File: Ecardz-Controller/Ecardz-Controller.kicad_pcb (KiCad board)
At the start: 4 copper layers, 189 x 115 mm, 165 parts, among them IC1 ST25R3916B-AQWT, J1 MEM2061-01-188-00-A, J2 Conn_01x04, J3 Conn_01x05, J4 Conn_01x09, J5 Conn_01x01, J6 Conn_01x24, J7 Conn_01x02, J8 Conn_01x04, J9 Conn_01x04, Q1 NMOS, U1 STM32G0C1RETx, U2 TPS62160DSG, U3 MIC5504-3.3YM5, U4 CP2110-F02-GM1, Y1 XRCGB27M120F3M00R0

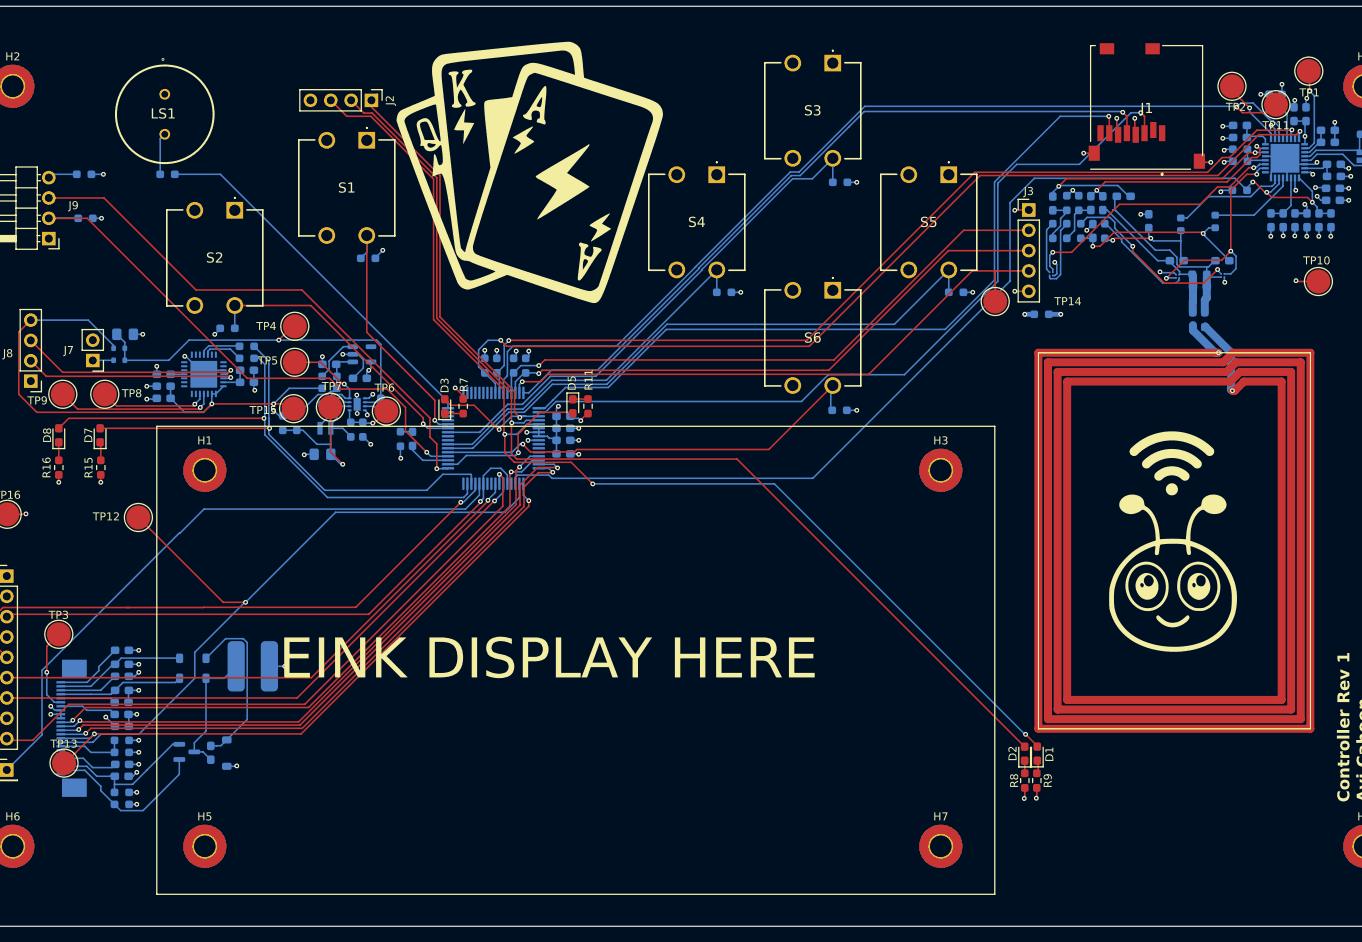
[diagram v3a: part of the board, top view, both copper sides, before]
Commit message: updates based on review
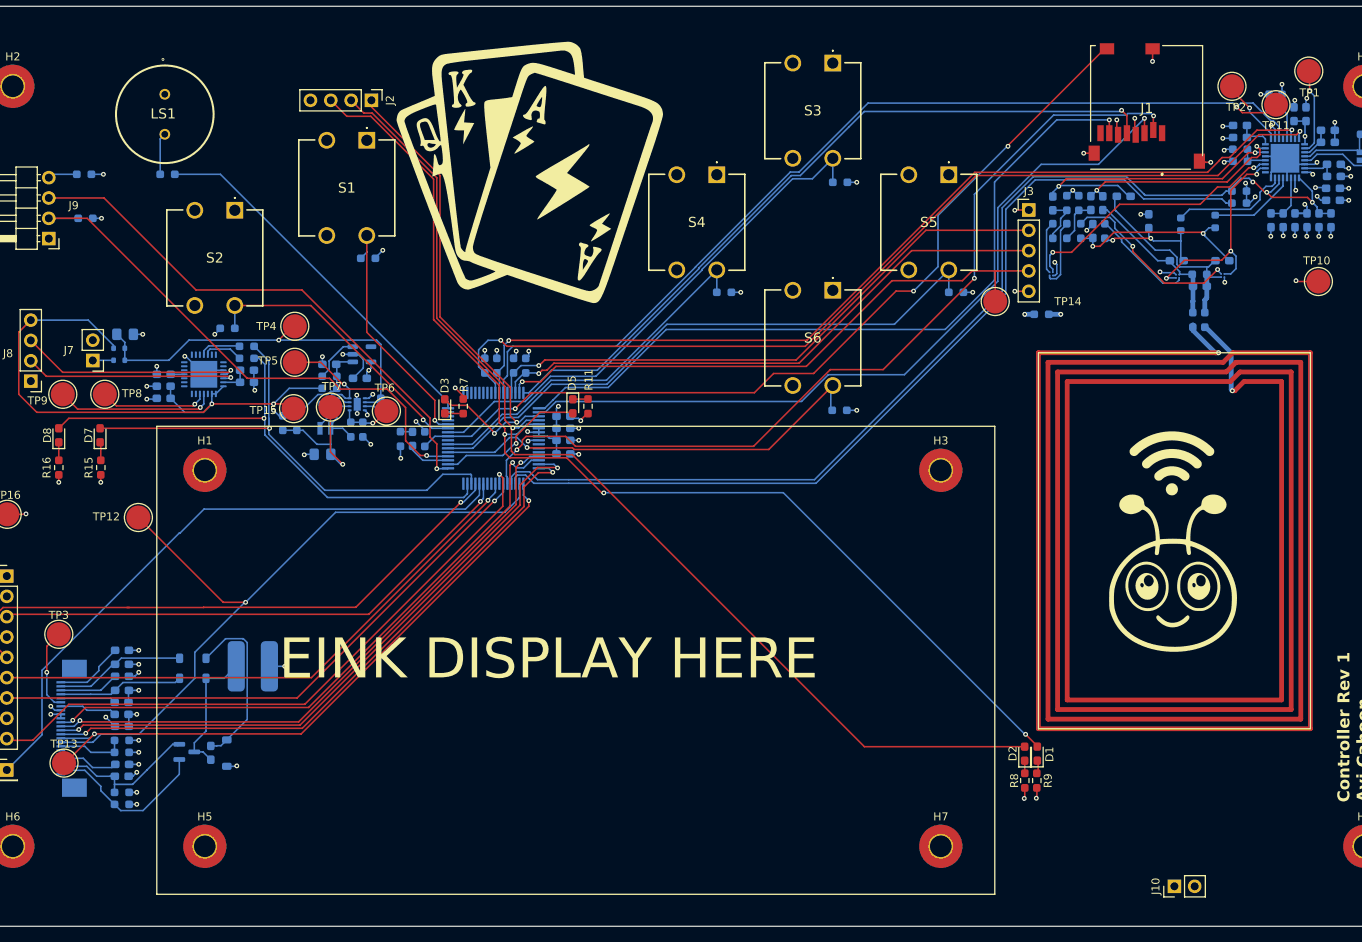
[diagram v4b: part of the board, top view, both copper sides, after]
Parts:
- added J10: Conn_01x02, Connector_PinHeader_2.54mm:PinHeader_1x02_P2.54mm_Vertical, F.Cu at (205.2, 200.0)
- added R50: 10k, Resistor_SMD:R_0603_1608Metric_Pad0.98x0.95mm_HandSolder, B.Cu at (111.5, 144.1)
- added R51: 0, Resistor_SMD:R_0603_1608Metric_Pad0.98x0.95mm_HandSolder, B.Cu at (213.3, 114.6)
- moved R2 0.12 mm to (213.3, 113.1), turned to 180 degrees
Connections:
- C6 pad 2: /MCU/NFC_I_SENSE -> /MCU/NFC_I_SENSE_P
- C8 pad 2: /MCU/NFC_I_SENSE -> /MCU/NFC_I_SENSE_P
- IC1 pad 14: /MCU/NFC_I_SENSE -> /MCU/NFC_I_SENSE_P
- IC1 pad 9: /MCU/NFC_I_SENSE -> /MCU/NFC_I_SENSE_P
- J1 pad CD1: unconnected-(J1-CARD_DETECT_1-PadCD1) -> GND
- J1 pad CD2: unconnected-(J1-CARD_DETECT_2-PadCD2) -> /MCU/SD_CARD_DETECT
- J4 pad 3: /MCU/SPI_LCD_CS -> /INTERFACE/SPI_LCD_CS
- R2 pad 2: /MCU/NFC_I_SENSE -> /MCU/NFC_I_SENSE_P
- U1 pad 19: /MCU/NFC_I_SENSE -> /MCU/NFC_I_SENSE_N
- U1 pad 20: unconnected-(U1-PA3-Pad20) -> /MCU/NFC_I_SENSE_P
- U1 pad 21: /MCU/SPI_LCD_CS -> /MCU/SD_CS
- U1 pad 27: /MCU/SPI_LCD_CS -> /INTERFACE/SPI_LCD_CS
- U1 pad 41: unconnected-(U1-PD9-Pad41) -> /MCU/SD_CARD_DETECT
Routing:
- net /MCU/NFC_I_SENSE_P: track 0.00 -> 137.1 mm, vias 0 -> 3
- net /MCU/NFC_I_SENSE: track 134.8 -> 0.00 mm, vias 3 -> 0
- net /MCU/NFC_I_SENSE_N: track 0.00 -> 114.0 mm
- net /MCU/SD_CS: track 0.00 -> 111.2 mm, vias 0 -> 3
- net /MCU/SD_CARD_DETECT: track 0.00 -> 109.9 mm, vias 0 -> 3
- net /MCU/SPI_LCD_CS: track 74.3 -> 0.00 mm, vias 1 -> 0
- net /INTERFACE/SPI_LCD_CS: track 0.00 -> 68.4 mm, vias 0 -> 1
- net VDD_NFC: track 21.7 -> 25.5 mm, vias 11 -> 12
- net /MCU/SD_MOSI: track 100.2 -> 97.7 mm
- net +3V3: track 30.3 -> 31.9 mm, vias 15 -> 16
- net GND: track 125.3 -> 126.7 mm, vias 77 -> 78
- net /INTERFACE/SDA: track 75.8 -> 77.0 mm
- net /MCU/LED_DISPLAY_R: track 19.7 -> 18.8 mm
- net /INTERFACE/BUTTON7: track 67.6 -> 68.3 mm
- net /MCU/SD_MISO: track 95.7 -> 95.1 mm
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
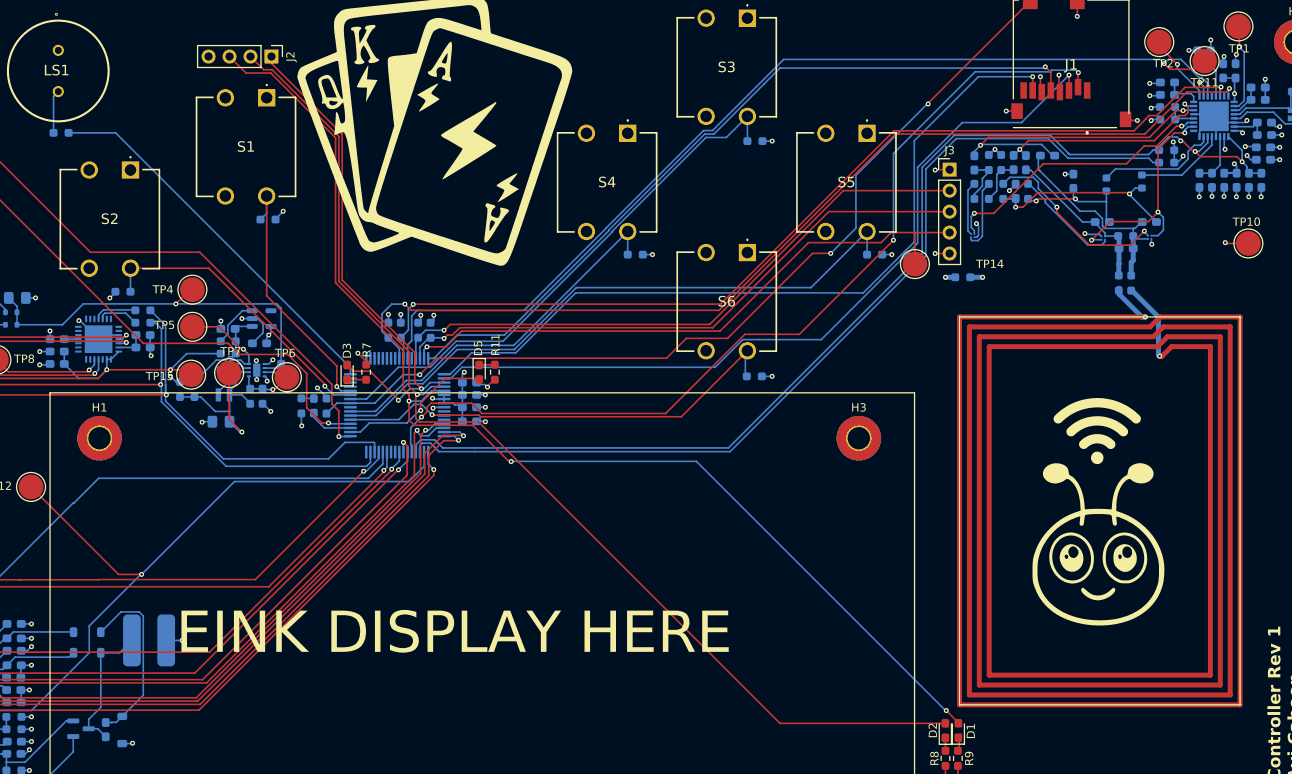
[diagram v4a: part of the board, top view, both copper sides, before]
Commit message: added current sense resistor and modified buzzer circuit
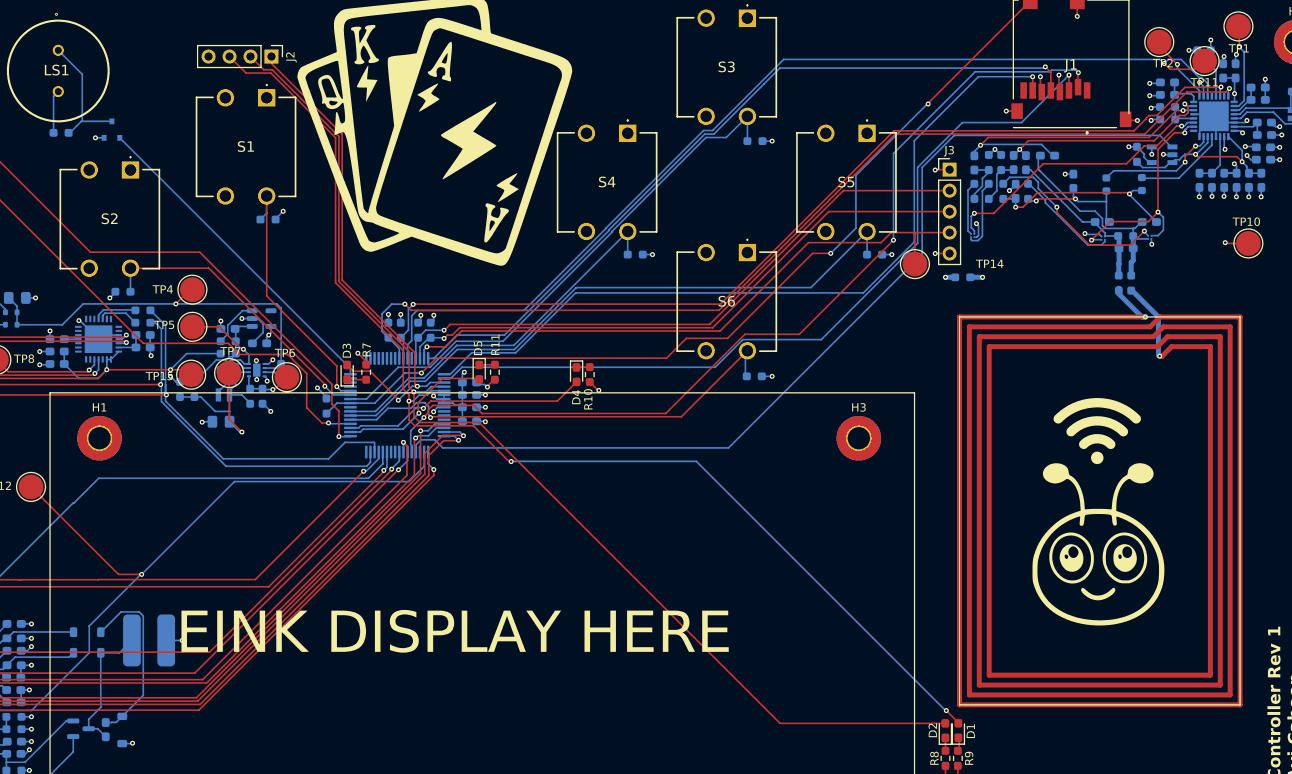
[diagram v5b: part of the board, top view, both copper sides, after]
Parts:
- removed R51: 0, Resistor_SMD:R_0603_1608Metric_Pad0.98x0.95mm_HandSolder
- added IC2: INA180A2IDBVR, samacsys:SOT95P280X145-5N, B.Cu at (212.8, 113.7)
- added Q2: TMBT3904,LM, samacsys:TMBT3904LM, B.Cu at (85.5, 110.6)
- D4, R10: moved to F.Cu
- moved R10 35.1 mm to (143.4, 140.3)
- moved D4 32.1 mm to (141.8, 140.3)
- moved R2 3.63 mm to (209.7, 113.6), turned to -90 degrees
- moved L3 0.30 mm to (210.3, 117.2)
- turned R19 to 0 degrees
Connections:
- C6 pad 2: /MCU/NFC_I_SENSE_P -> Net-(IC1-VDD_DR)
- C8 pad 2: /MCU/NFC_I_SENSE_P -> Net-(IC1-VDD_DR)
- IC1 pad 14: /MCU/NFC_I_SENSE_P -> Net-(IC1-VDD_DR)
- IC1 pad 9: /MCU/NFC_I_SENSE_P -> Net-(IC1-VDD_DR)
- LS1 pad 1: GND -> Net-(Q2-C)
- LS1 pad 2: Net-(LS1-Pad2) -> +3V3
- R19 pad 1: /INTERFACE/BUZZER -> +3V3
- R19 pad 2: Net-(LS1-Pad2) -> Net-(Q2-C)
- R2 pad 2: /MCU/NFC_I_SENSE_P -> Net-(IC1-VDD_DR)
- U1 pad 19: /MCU/NFC_I_SENSE_N -> unconnected-(U1-PA2-Pad19)
- U1 pad 20: /MCU/NFC_I_SENSE_P -> /MCU/NFC_I_SENSE
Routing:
- net /MCU/NFC_I_SENSE_P: track 137.1 -> 0.00 mm, vias 3 -> 0
- net /MCU/NFC_I_SENSE: track 0.00 -> 115.5 mm
- net /MCU/NFC_I_SENSE_N: track 114.0 -> 0.00 mm
- net Net-(IC1-VDD_DR): track 0.00 -> 24.7 mm, vias 0 -> 2
- net /MCU/LED_DISPLAY_B: track 5.49 -> 29.9 mm, vias 0 -> 1
- net Net-(Q2-C): track 0.00 -> 15.6 mm
- net /INTERFACE/BUZZER: track 46.7 -> 40.3 mm
- net +3V3: track 31.9 -> 37.3 mm
- net Net-(LS1-Pad2): track 5.24 -> 0.00 mm
- net GND: track 126.7 -> 129.0 mm, vias 78 -> 80
- net /INTERFACE/SDA: track 77.0 -> 75.9 mm
- net /INTERFACE/BUTTON6: track 56.0 -> 56.9 mm
- net /MCU/SD_CS: track 111.2 -> 110.7 mm
- net VDD_NFC: track 25.5 -> 25.0 mm
- net /MCU/LED_DEBUG_B: track 63.3 -> 62.8 mm
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
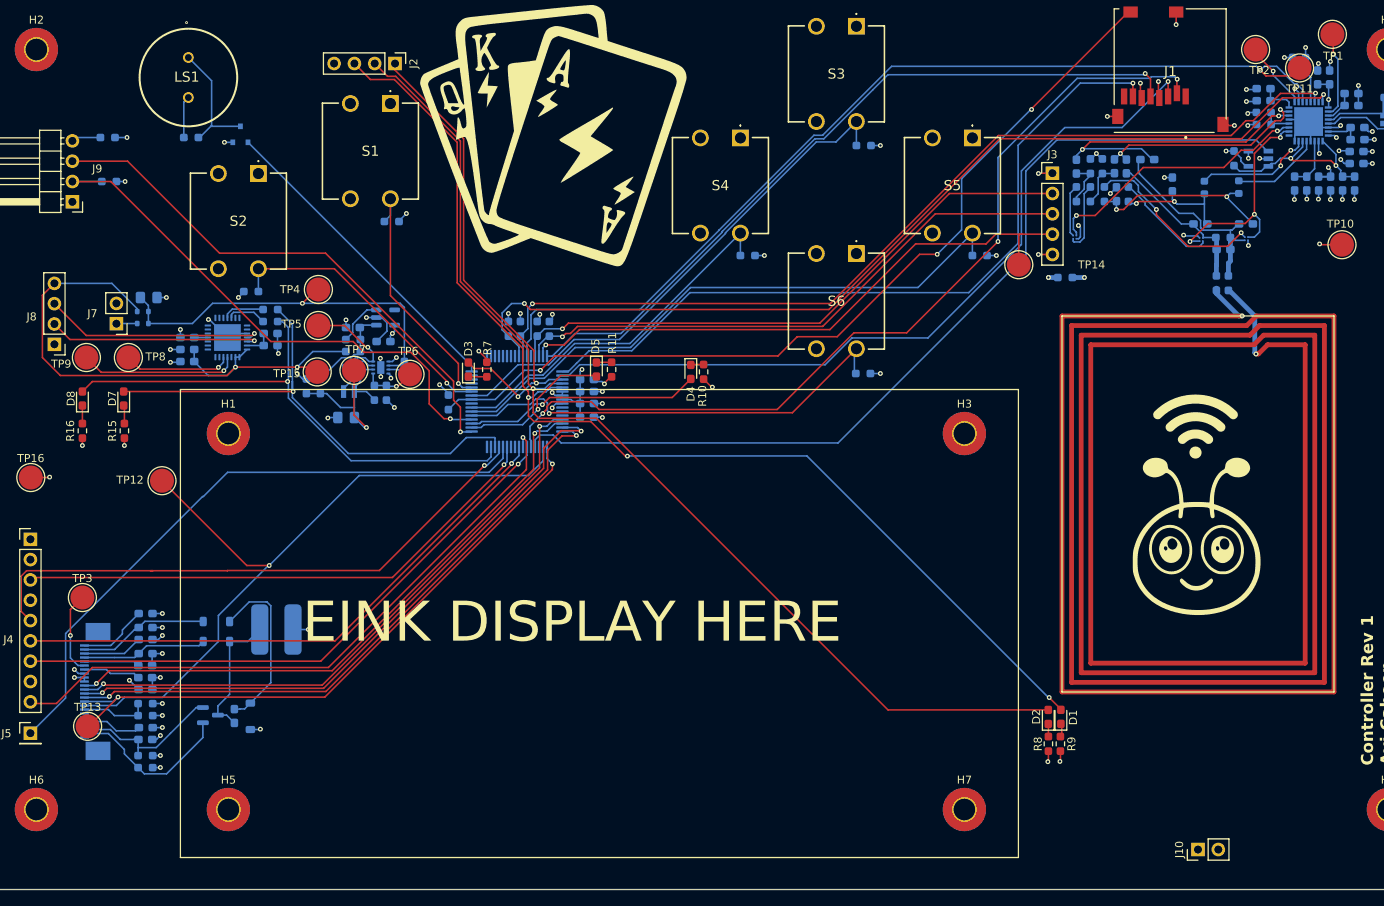
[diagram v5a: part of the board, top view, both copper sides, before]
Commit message: updated layout for new mcu pin assignments
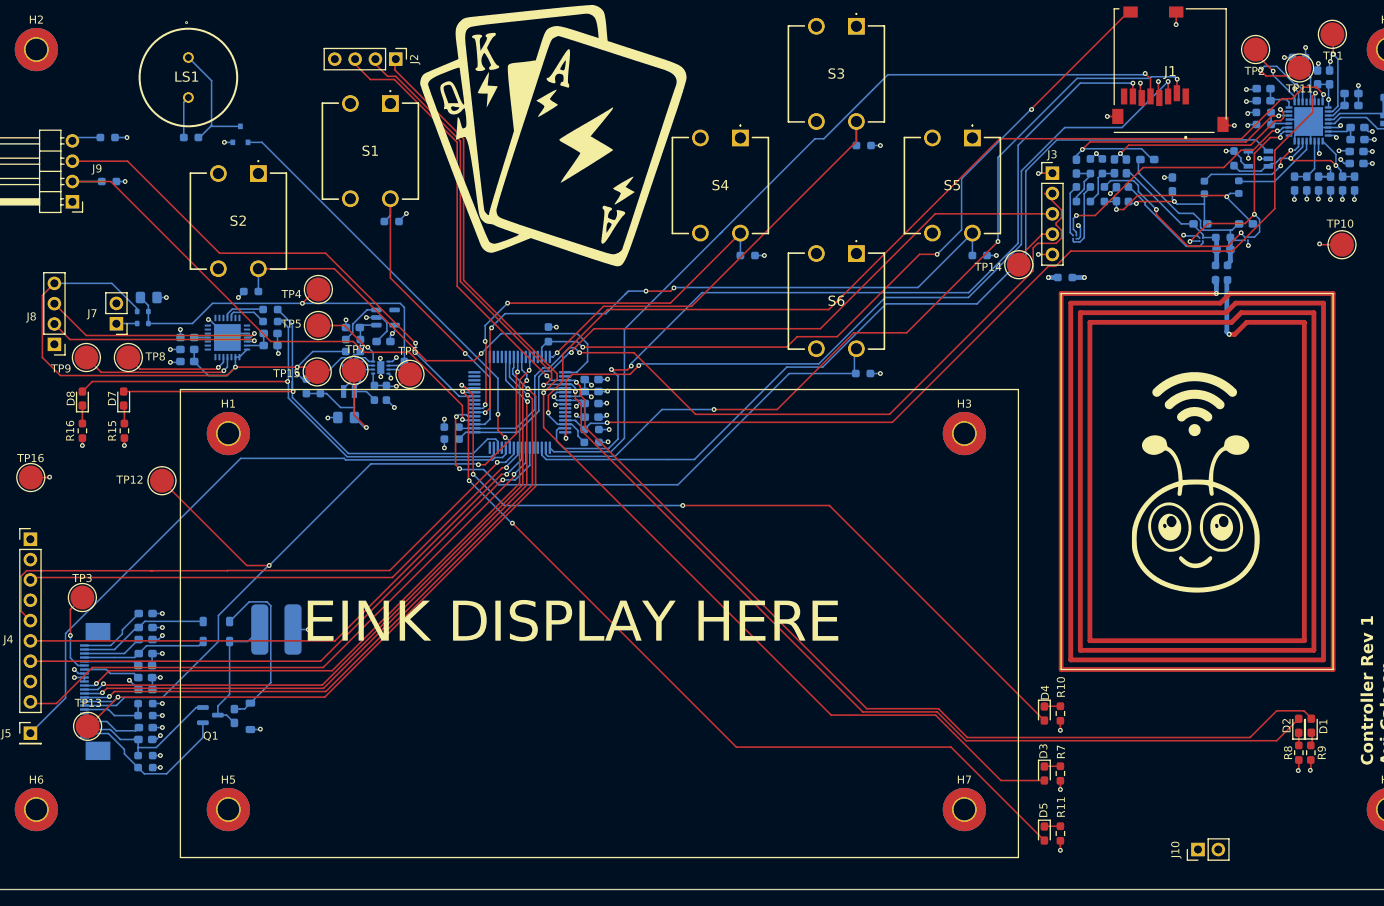
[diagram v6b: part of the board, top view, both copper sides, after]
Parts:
- moved D3 87.9 mm to (186.0, 190.5), turned to -90 degrees
- moved R7 87.7 mm to (188.0, 190.5), turned to -90 degrees
- moved R11 80.7 mm to (188.0, 198.0)
- moved D5 80.6 mm to (186.0, 198.0)
- moved R10 61.8 mm to (188.0, 183.0)
- moved D4 61.5 mm to (186.0, 183.0)
- moved R8 31.3 mm to (217.8, 187.9)
- moved R9 31.3 mm to (219.3, 187.9)
- moved D1 31.3 mm to (219.4, 184.5)
- moved D2 31.3 mm to (217.8, 184.5)
- moved R17 18.4 mm to (111.9, 148.7), turned to 0 degrees
- moved R14 17.6 mm to (129.4, 149.1), turned to 180 degrees
- moved R18 16.3 mm to (111.9, 147.2), turned to 0 degrees
- moved R13 15.4 mm to (129.4, 147.5), turned to 180 degrees
- moved R50 15.1 mm to (124.0, 135.6)
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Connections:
- IC1 pad 27: /MCU/NFC_BUSY -> /MCU/NFC_A_BUSY
- IC1 pad 30: /MCU/I2C_NFC_SCL -> /MCU/NFC_A_SCL
- IC1 pad 32: /MCU/I2C_NFC_SDA -> /MCU/NFC_A_SDA
- J4 pad 3: /INTERFACE/SPI_LCD_CS -> /MCU/SPI_LCD_CS
- J4 pad 5: /INTERFACE/SPI_LCD_DC -> /MCU/SPI_LCD_DC
- R13 pad 2: /MCU/I2C_NFC_SCL -> /MCU/NFC_A_SCL
- R14 pad 2: /MCU/I2C_NFC_SDA -> /MCU/NFC_A_SDA
- TP11 pad 1: /MCU/NFC_BUSY -> /MCU/NFC_A_BUSY
- U1 pad 1: /MCU/SD_MISO -> /INTERFACE/BUTTON2
- U1 pad 13: /INTERFACE/SCL -> /MCU/NFC_A_SCL
- U1 pad 14: /INTERFACE/SDA -> /MCU/NFC_A_SDA
- U1 pad 15: /INTERFACE/CS# -> /MCU/SD_MISO
- U1 pad 16: /INTERFACE/D/C# -> /MCU/SD_MOSI
- U1 pad 17: /INTERFACE/RES# -> /MCU/SD_SCK
- U1 pad 18: /INTERFACE/BUSY -> /MCU/SD_CS
- U1 pad 19: unconnected-(U1-PA2-Pad19) -> /MCU/NFC_I_SENSE
- U1 pad 2: /MCU/SD_MOSI -> unconnected-(U1-PC12-Pad2)
- U1 pad 20: /MCU/NFC_I_SENSE -> unconnected-(U1-PA3-Pad20)
- U1 pad 21: /MCU/SD_CS -> unconnected-(U1-PA4-Pad21)
- U1 pad 25: unconnected-(U1-PC4-Pad25) -> /MCU/SPI_LCD_CS
- U1 pad 26: unconnected-(U1-PC5-Pad26) -> /MCU/SPI_LCD_DC
- U1 pad 27: /INTERFACE/SPI_LCD_CS -> /INTERFACE/BUZZER
- U1 pad 29: /INTERFACE/SPI_LCD_DC -> unconnected-(U1-PB2-Pad29)
- U1 pad 3: /MCU/LED_DEBUG_B -> /MCU/LED_NFC_DONE
- U1 pad 33: /MCU/PWR_INDICATOR -> /MCU/NFC_B_SCL
- U1 pad 34: /MCU/LED_DISPLAY_R -> /MCU/NFC_B_SDA
- U1 pad 35: /MCU/LED_DISPLAY_B -> /INTERFACE/BUTTON1
- U1 pad 41: /MCU/SD_CARD_DETECT -> unconnected-(U1-PD9-Pad41)
- U1 pad 42: /INTERFACE/BUTTON3 -> /MCU/PWR_INDICATOR
- U1 pad 43: /INTERFACE/BUTTON2 -> /MCU/LED_DISPLAY_R
- U1 pad 44: /INTERFACE/BUTTON1 -> /MCU/LED_DISPLAY_B
- U1 pad 48: /INTERFACE/BUZZER -> unconnected-(U1-PC8-Pad48)
- U1 pad 5: /MCU/LED_NFC_DONE -> /MCU/LED_DEBUG_B
- U1 pad 53: unconnected-(U1-PD3-Pad53) -> /INTERFACE/CS#
- U1 pad 54: unconnected-(U1-PD4-Pad54) -> /INTERFACE/D/C#
- U1 pad 55: unconnected-(U1-PD5-Pad55) -> /INTERFACE/RES#
- U1 pad 56: unconnected-(U1-PD6-Pad56) -> /INTERFACE/BUSY
- U1 pad 57: /MCU/I2C_NFC_SDA -> /INTERFACE/SCL
- U1 pad 58: /MCU/I2C_NFC_SCL -> /MCU/SPI_EINK_MISO
- U1 pad 59: /MCU/NFC_BUSY -> /INTERFACE/SDA
- U1 pad 61: /MCU/NFC_B_SDA -> unconnected-(U1-PB7-Pad61)
- U1 pad 62: /MCU/NFC_B_SCL -> /MCU/SD_CARD_DETECT
- U1 pad 63: /MCU/NFC_B_BUSY -> unconnected-(U1-PB9-Pad63)
- U1 pad 64: /MCU/SD_SCK -> /INTERFACE/BUTTON3
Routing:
- net /MCU/NFC_A_SDA: track 0.00 -> 124.9 mm, vias 0 -> 2
- net /MCU/NFC_BUSY: track 123.5 -> 0.00 mm, vias 1 -> 0
- net /MCU/I2C_NFC_SDA: track 122.1 -> 0.00 mm, vias 2 -> 0
- net /MCU/NFC_A_SCL: track 0.00 -> 118.3 mm, vias 0 -> 2
- net /MCU/I2C_NFC_SCL: track 116.9 -> 0.00 mm, vias 2 -> 0
- net /MCU/LED_DISPLAY_R: track 19.2 -> 103.5 mm, vias 1 -> 3
- net /MCU/LED_DEBUG_B: track 62.8 -> 139.5 mm, vias 2 -> 1
- net /MCU/SPI_LCD_DC: track 0.00 -> 75.1 mm, vias 0 -> 1
- net /INTERFACE/SPI_LCD_DC: track 73.2 -> 0.00 mm, vias 1 -> 0
- net /INTERFACE/SPI_LCD_CS: track 68.4 -> 0.00 mm, vias 1 -> 0
- net /MCU/SPI_LCD_CS: track 0.00 -> 68.4 mm, vias 0 -> 1
- net /MCU/NFC_B_BUSY: track 74.5 -> 6.31 mm, vias 1 -> 0
- net /MCU/LED_DISPLAY_B: track 29.9 -> 97.7 mm, vias 1 -> 3
- net /MCU/LED_NFC_WORKING: track 136.1 -> 167.1 mm, vias 1 -> 2
- net /MCU/NFC_B_SDA: track 74.4 -> 104.1 mm
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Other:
- board text added: "R31"
